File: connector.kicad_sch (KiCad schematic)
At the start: 1 part, among them J3 trionic5_header

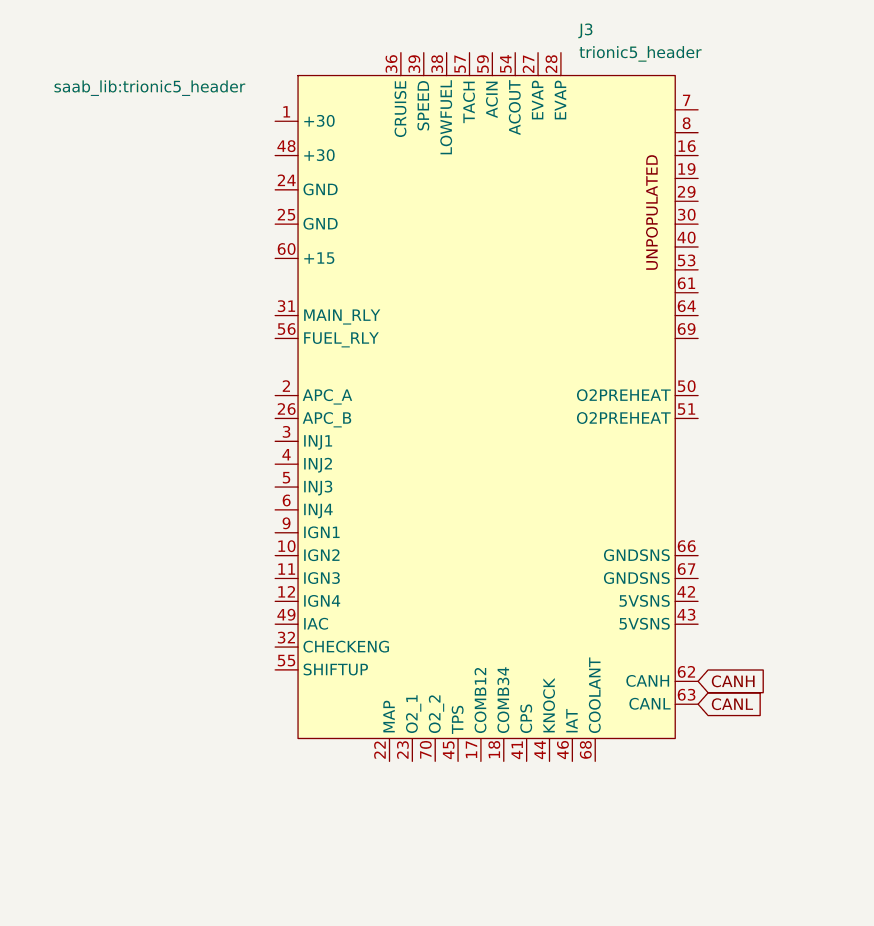
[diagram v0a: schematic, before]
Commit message: Boards should be placed correctly now
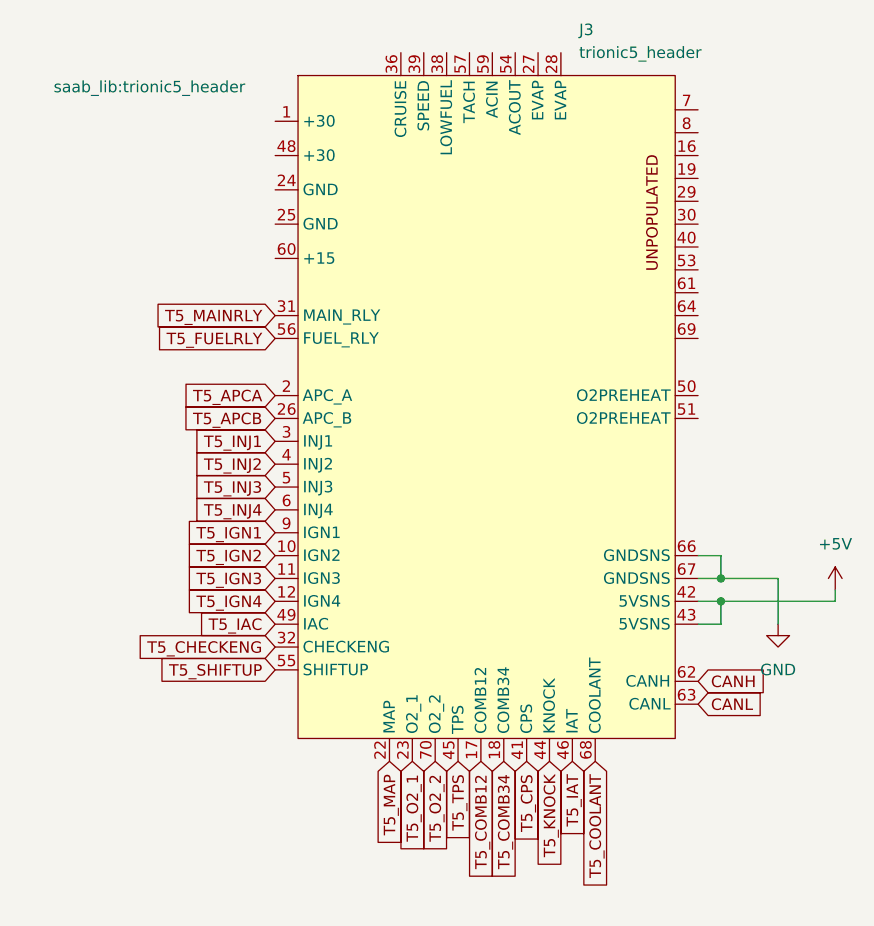
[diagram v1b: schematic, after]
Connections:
- net T5_IGN2: now reaches J3.10 (IGN2)
- net T5_IGN3: now reaches J3.11 (IGN3)
- net T5_IGN4: now reaches J3.12 (IGN4)
- net T5_COMB12: now reaches J3.17 (COMB12)
- net T5_COMB34: now reaches J3.18 (COMB34)
- net T5_APCA: now reaches J3.2 (APC_A)
- net T5_MAP: now reaches J3.22 (MAP)
- net T5_O2_1: now reaches J3.23 (O2_1)
- net T5_APCB: now reaches J3.26 (APC_B)
- net T5_INJ1: now reaches J3.3 (INJ1)
- net T5_MAINRLY: now reaches J3.31 (MAIN_RLY)
- net T5_CHECKENG: now reaches J3.32 (CHECKENG)
- net T5_INJ2: now reaches J3.4 (INJ2)
- net T5_CPS: now reaches J3.41 (CPS)
- net +5V: now reaches J3.42 (5VSNS)
- net +5V: now also J3.43 (5VSNS)
- net T5_KNOCK: now reaches J3.44 (KNOCK)
- net T5_TPS: now reaches J3.45 (TPS)
- net T5_IAT: now reaches J3.46 (IAT)
- net T5_IAC: now reaches J3.49 (IAC)
- net T5_INJ3: now reaches J3.5 (INJ3)
- net T5_SHIFTUP: now reaches J3.55 (SHIFTUP)
- net T5_FUELRLY: now reaches J3.56 (FUEL_RLY)
- net T5_INJ4: now reaches J3.6 (INJ4)
- net GND: now reaches J3.66 (GNDSNS)
- net GND: now also J3.67 (GNDSNS)
- net T5_COOLANT: now reaches J3.68 (COOLANT)
- net T5_O2_2: now reaches J3.70 (O2_2)
- net T5_IGN1: now reaches J3.9 (IGN1)

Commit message: More changes
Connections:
- net GND: now also J3.24 (GND), J3.25 (GND)
- net +30: now reaches J3.1 (+30)
- net +30: now also J3.48 (+30)
- net T5_WBO2: now reaches J3.19
- net +15: now reaches J3.60 (+15)
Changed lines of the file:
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@@
   (junction (at 105.41 81.28) (diameter 0) (color 0 0 0 0)
   )
+  (junction (at 53.34 41.91) (diameter 0) (color 0 0 0 0)
+  )
   (junction (at 105.41 83.82) (diameter 0) (color 0 0 0 0)
   )
+  (junction (at 53.34 30.48) (diameter 0) (color 0 0 0 0)
+  )
+  (wire (pts (xy 53.34 30.48) (xy 53.34 34.29))
+    (stroke (width 0) (type default) (color 0 0 0 0))
+  )
+  (wire (pts (xy 53.34 38.1) (xy 55.88 38.1))
+    (stroke (width 0) (type default) (color 0 0 0 0))
+  )
+  (wire (pts (xy 36.83 43.18) (xy 36.83 41.91))
+    (stroke (width 0) (type default) (color 0 0 0 0))
+  )
+  (wire (pts (xy 53.34 34.29) (xy 55.88 34.29))
+    (stroke (width 0) (type default) (color 0 0 0 0))
+  )
   (wire (pts (xy 118.11 83.82) (xy 118.11 82.55))
     (stroke (width 0) (type default) (color 0 0 0 0))
@@
     (stroke (width 0) (type default) (color 0 0 0 0))
   )
+  (wire (pts (xy 55.88 41.91) (xy 53.34 41.91))
+    (stroke (width 0) (type default) (color 0 0 0 0))
+  )
+  (wire (pts (xy 53.34 41.91) (xy 53.34 38.1))
+    (stroke (width 0) (type default) (color 0 0 0 0))
+  )
+  (wire (pts (xy 53.34 30.48) (xy 55.88 30.48))
+    (stroke (width 0) (type default) (color 0 0 0 0))
+  )
   (wire (pts (xy 102.87 78.74) (xy 105.41 78.74))
     (stroke (width 0) (type default) (color 0 0 0 0))
   )
+  (wire (pts (xy 36.83 41.91) (xy 53.34 41.91))
+    (stroke (width 0) (type default) (color 0 0 0 0))
+  )
   (wire (pts (xy 102.87 83.82) (xy 105.41 83.82))
     (stroke (width 0) (type default) (color 0 0 0 0))
   )
   (wire (pts (xy 102.87 86.36) (xy 105.41 86.36))
+    (stroke (width 0) (type default) (color 0 0 0 0))
+  )
+  (wire (pts (xy 48.26 30.48) (xy 53.34 30.48))
     (stroke (width 0) (type default) (color 0 0 0 0))
   )
@@
     )
   )
+  (global_label "+15" (shape input) (at 55.88 45.72 180) (fields_autoplaced)
+    (effects (font (size 1.27 1.27)) (justify right))
+    (property "Intersheet References" "${INTERSHEET_REFS}" (id 0) (at 49.5644 45.6406 0)
+      (effects (font (size 1.27 1.27)) (justify right) hide)
+    )
+  )
   (global_label "T5_APCB" (shape input) (at 55.88 63.5 180) (fields_autoplaced)
     (effects (font (size 1.27 1.27)) (justify right))
@@
     )
   )
+  (global_label "+30" (shape input) (at 48.26 30.48 180) (fields_autoplaced)
+    (effects (font (size 1.27 1.27)) (justify right))
+    (property "Intersheet References" "${INTERSHEET_REFS}" (id 0) (at 41.9444 30.4006 0)
+      (effects (font (size 1.27 1.27)) (justify right) hide)
+    )
+  )
   (global_label "T5_INJ4" (shape input) (at 55.88 73.66 180) (fields_autoplaced)
     (effects (font (size 1.27 1.27)) (justify right))
     (property "Intersheet References" "${INTERSHEET_REFS}" (id 0) (at 46.2987 73.5806 0)
       (effects (font (size 1.27 1.27)) (justify right) hide)
+    )
+  )
+  (global_label "T5_WBO2" (shape input) (at 102.87 36.83 0) (fields_autoplaced)
+    (effects (font (size 1.27 1.27)) (justify left))
+    (property "Intersheet References" "${INTERSHEET_REFS}" (id 0) (at 113.6004 36.7506 0)
+      (effects (font (size 1.27 1.27)) (justify left) hide)
     )
   )
@@
       (effects (font (size 1.27 1.27)) hide)
     )
+    (pin "1")
+  )
+  (symbol (lib_id "power:GND") (at 36.83 43.18 0) (unit 1)
+    (in_bom yes) (on_board yes) (fields_autoplaced)
+    (property "Reference" "#PWR0153" (id 0) (at 36.83 49.53 0)
+      (effects (font (size 1.27 1.27)) hide)
+    )
+    (property "Value" "GND" (id 1) (at 36.83 48.26 0))
+    (property "Footprint" "" (id 2) (at 36.83 43.18 0)
+      (effects (font (size 1.27 1.27)) hide)
+    )
+    (property "Datasheet" "" (id 3) (at 36.83 43.18 0)
+      (effects (font (size 1.27 1.27)) hide)
+    )
